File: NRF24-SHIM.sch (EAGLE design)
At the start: 21 parts

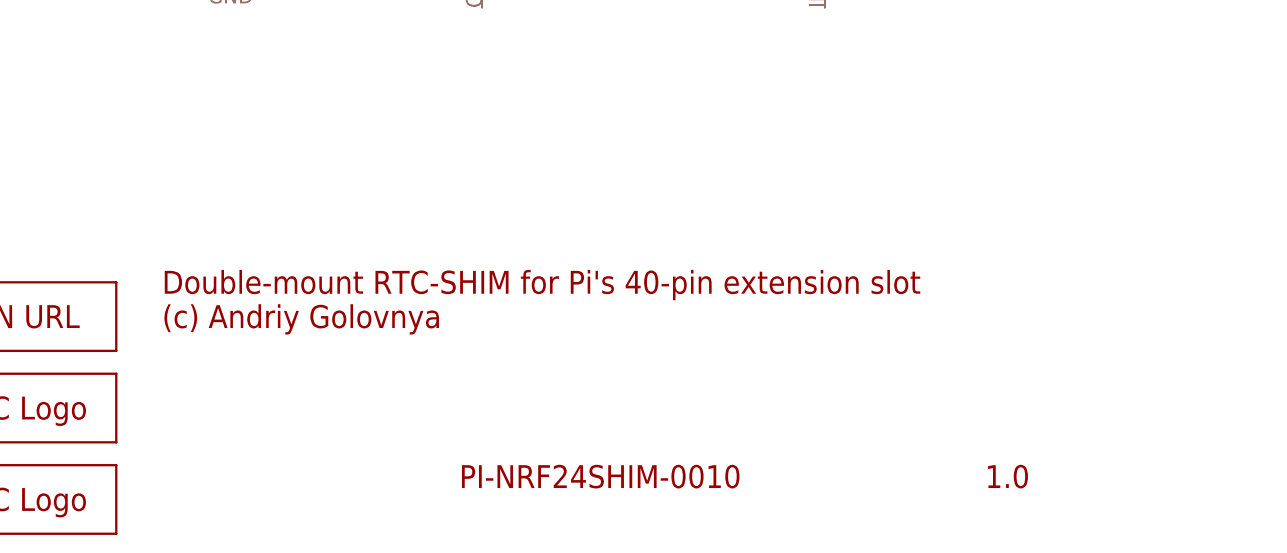
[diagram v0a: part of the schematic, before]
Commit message: Moved some traces around. Fixed schematics description.
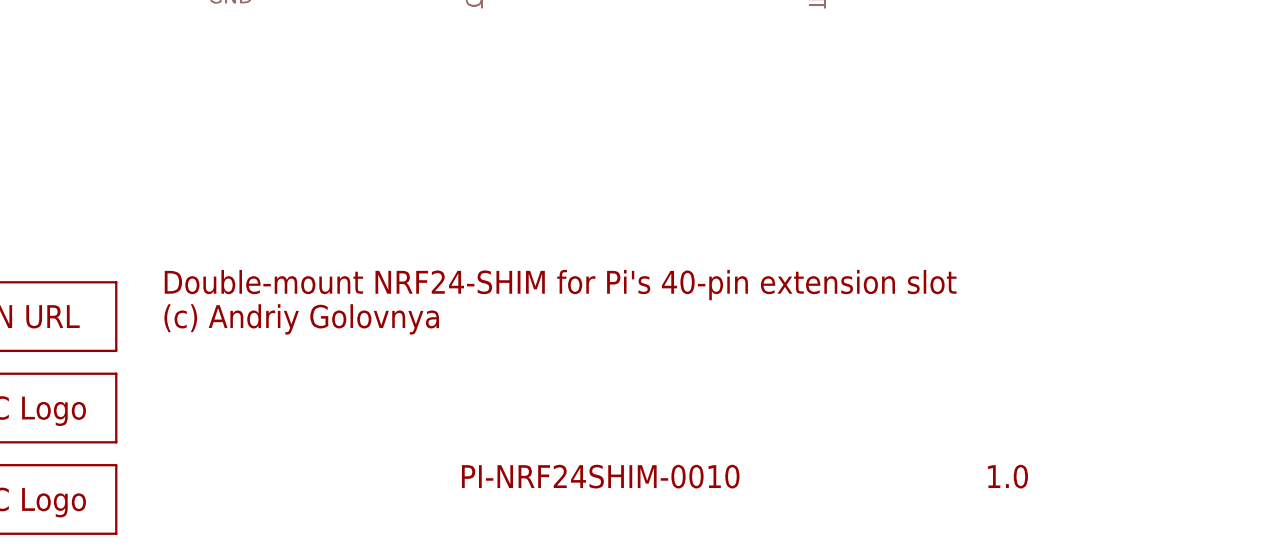
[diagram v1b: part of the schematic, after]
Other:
- note added: "Double-mount NRF24-SHIM for Pi's 40-pin extension slot (c) Andriy Golovnya"
- note removed: "Double-mount RTC-SHIM for Pi's 40-pin extension slot (c) Andriy Golovnya"
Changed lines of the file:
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@@
 <text x="256.54" y="7.62" size="2.54" layer="94">1.0</text>
 <text x="198.12" y="7.62" size="2.54" layer="94">PI-NRF24SHIM-0010</text>
-<text x="165.1" y="25.4" size="2.54" layer="94">Double-mount RTC-SHIM for Pi's 40-pin extension slot
+<text x="165.1" y="25.4" size="2.54" layer="94">Double-mount NRF24-SHIM for Pi's 40-pin extension slot
 (c) Andriy Golovnya</text>
 <text x="40.64" y="129.54" size="2.54" layer="94">NRF24 connector</text>

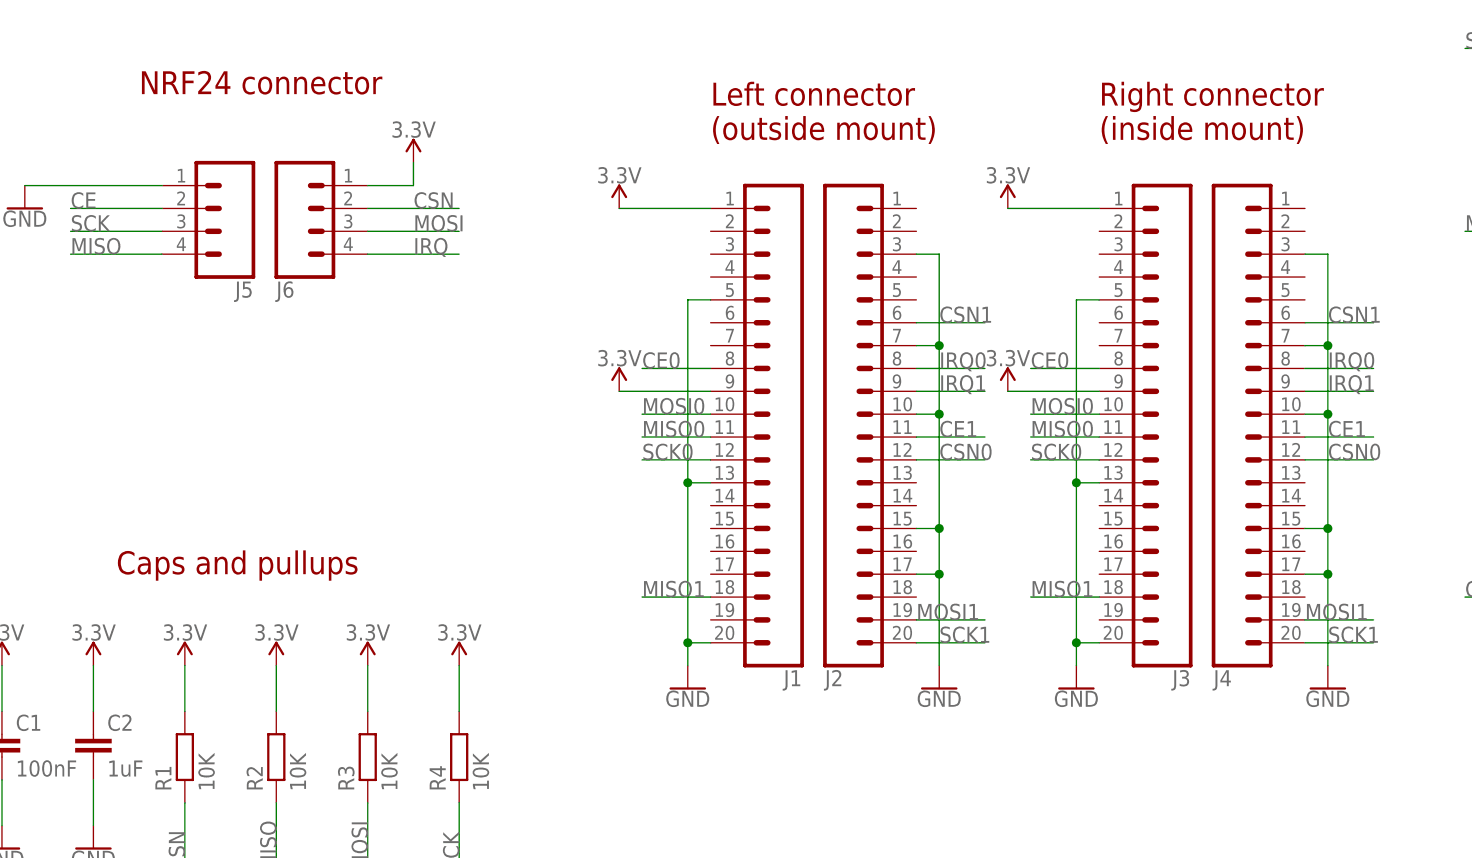
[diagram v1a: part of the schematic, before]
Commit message: Use more locking pin headers. Moved some traces.
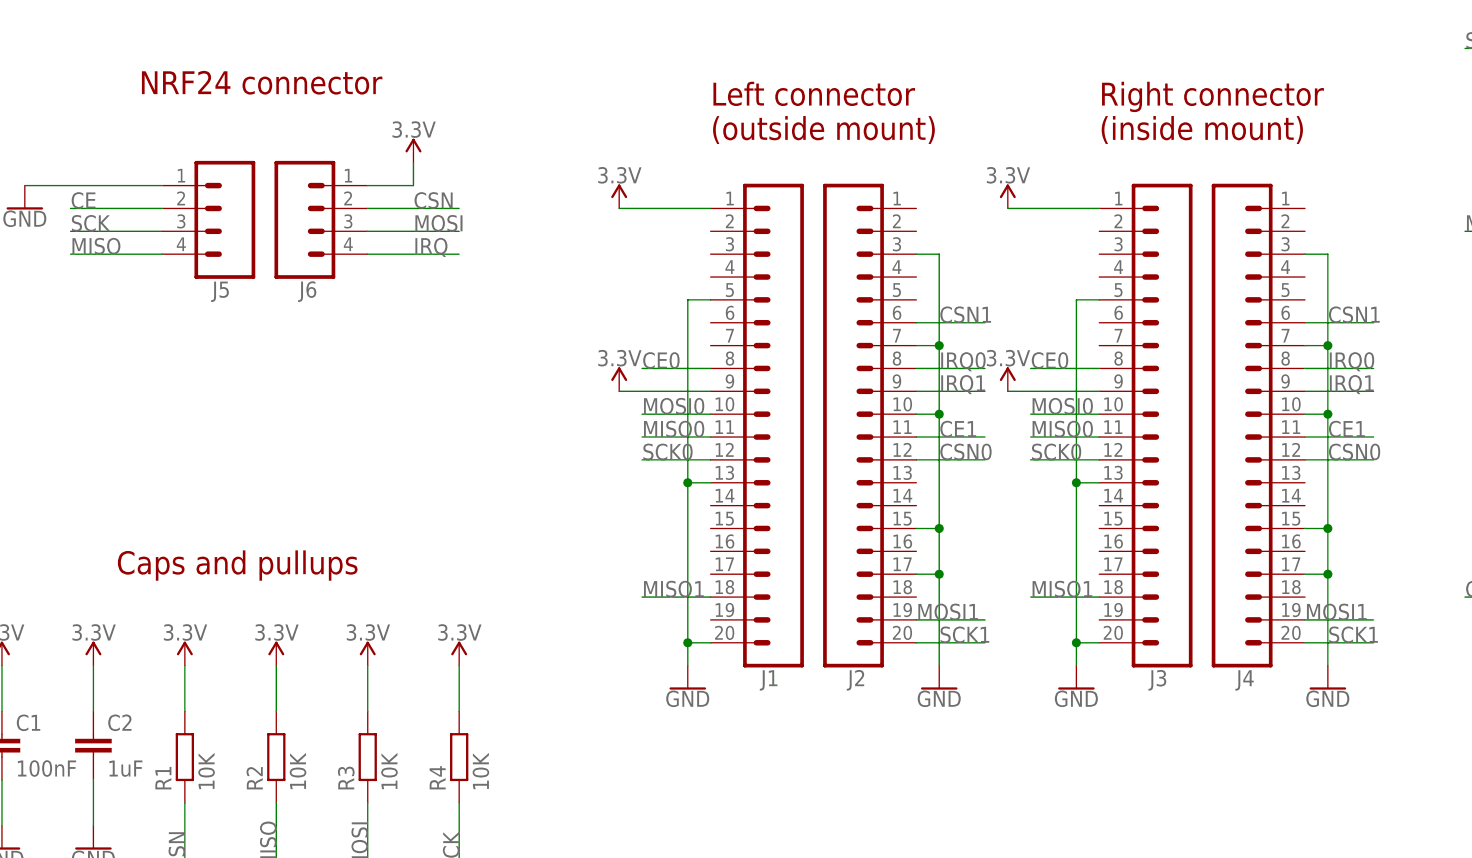
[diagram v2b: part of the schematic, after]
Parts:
- J1, J2, J3, J4: device SparkFun-Connectors:CONN_20LOCK_NOSILK -> _my_locked_connectors:CONN_20LOCK
- J5, J6: device SparkFun-Connectors:CONN_04LOCK -> _my_locked_connectors:CONN_04LOCK

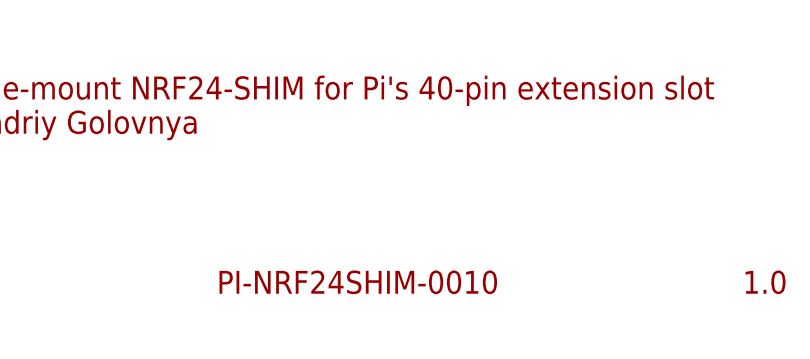
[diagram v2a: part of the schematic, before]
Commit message: Simplified document names. Generated PDF schematics.
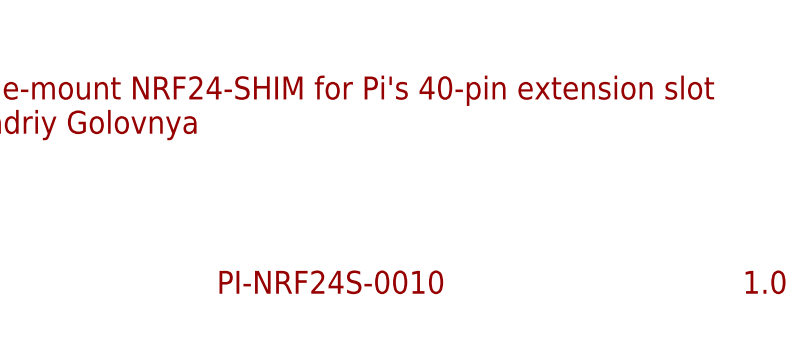
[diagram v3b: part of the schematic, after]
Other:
- note added: "PI-NRF24S-0010"
- note removed: "PI-NRF24SHIM-0010"
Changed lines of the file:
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@@
 <plain>
 <text x="256.54" y="7.62" size="2.54" layer="94">1.0</text>
-<text x="198.12" y="7.62" size="2.54" layer="94">PI-NRF24SHIM-0010</text>
+<text x="198.12" y="7.62" size="2.54" layer="94">PI-NRF24S-0010</text>
 <text x="165.1" y="25.4" size="2.54" layer="94">Double-mount NRF24-SHIM for Pi's 40-pin extension slot
 (c) Andriy Golovnya</text>
